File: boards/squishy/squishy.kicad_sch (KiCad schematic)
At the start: 66 parts, among them J10 QXH-060, J2 Conn_02x20_Odd_Even_Shielded, J8 TRIGGER, J9 REFCLK, SW2 DFU, U1 LFE5UM5G-45F-8BG381C, U2 GD25Q64EWIGR, U6 ATSAMD09D14A-M, X1 48MHz

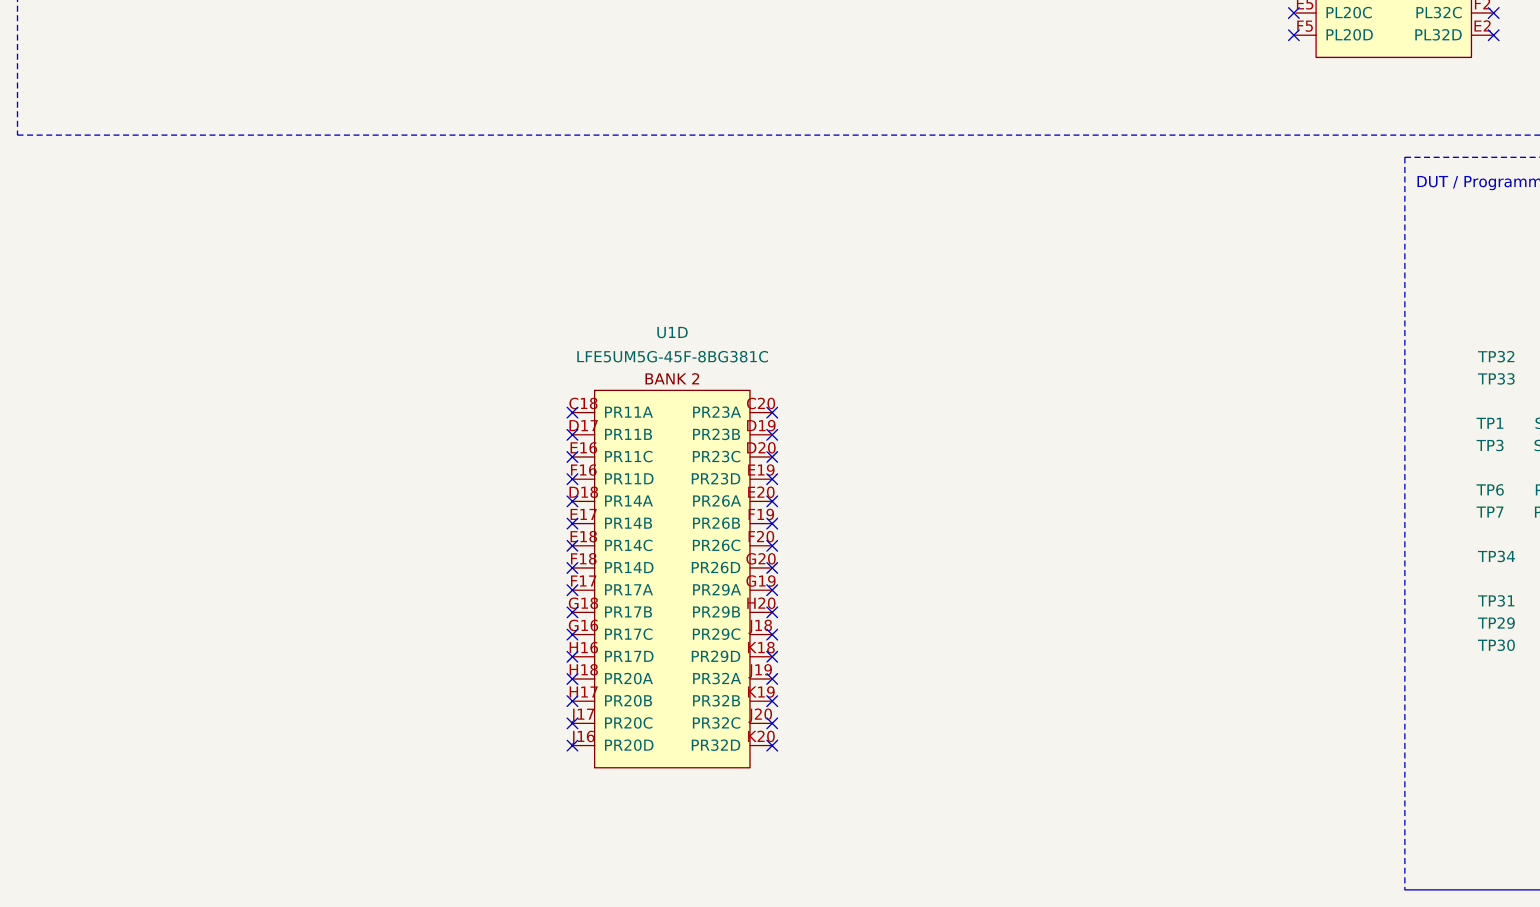
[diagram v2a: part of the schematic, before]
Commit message: hardware: squishy: added the microSD card slot
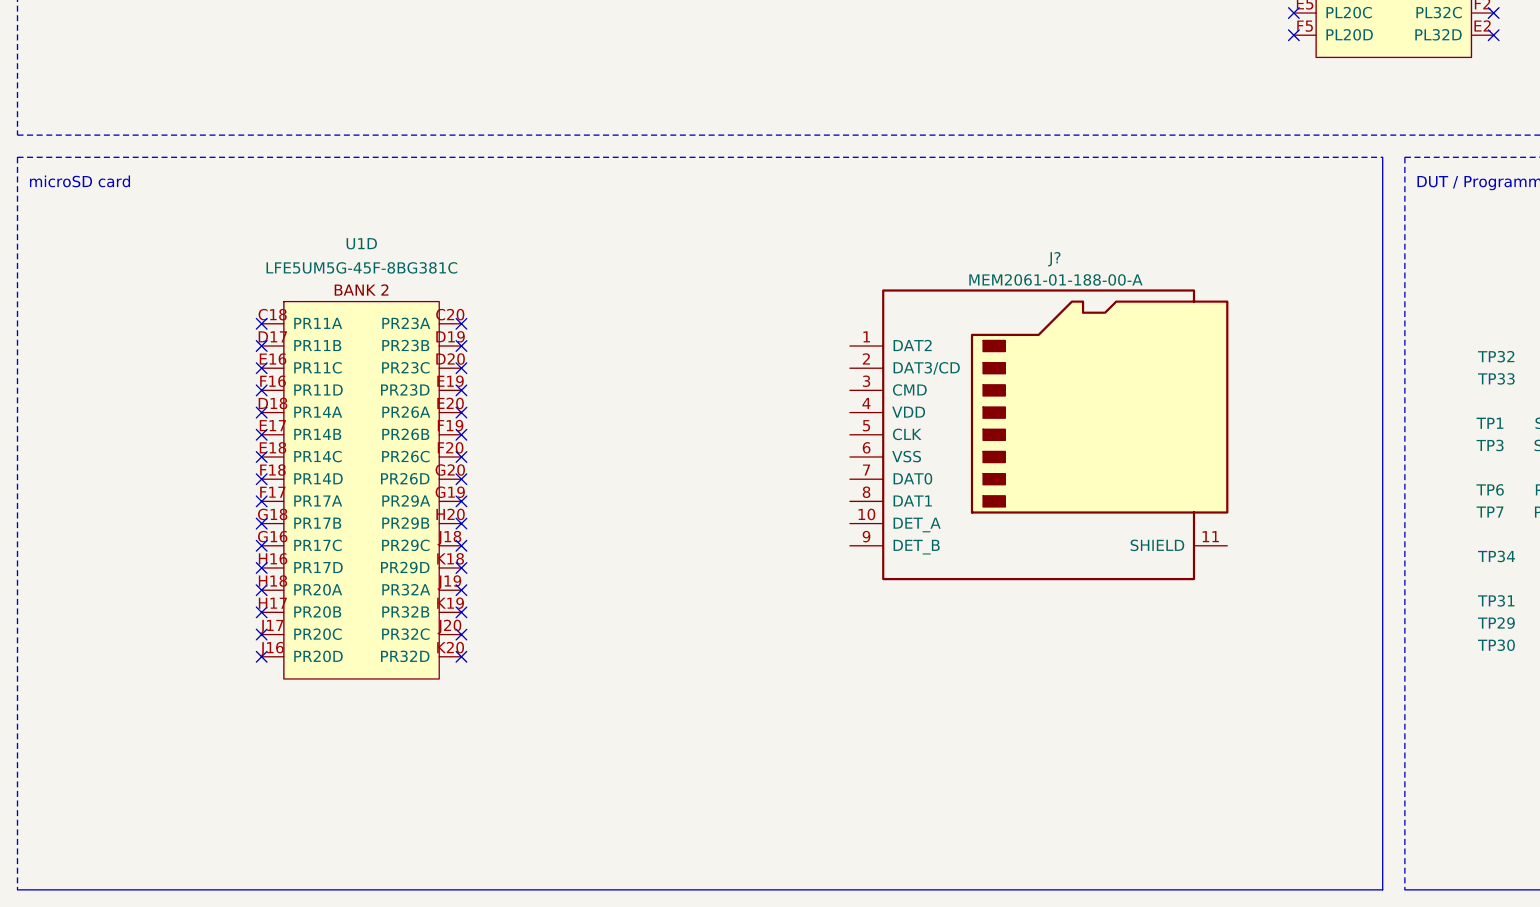
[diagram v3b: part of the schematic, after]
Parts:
- added J?: MEM2061-01-188-00-A, lethalbit-connectors:GCT_MEM2061-01-188-00-A_REVA, symbol Connector:Micro_SD_Card_Det
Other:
- note added: "microSD card"
- moved on the sheet: U1D
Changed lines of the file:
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@@
   (no_connect (at 290.83 93.98))
   (no_connect (at 290.83 78.74))
-  (no_connect (at 100.33 256.54))
-  (no_connect (at 100.33 254))
-  (no_connect (at 100.33 264.16))
-  (no_connect (at 100.33 261.62))
-  (no_connect (at 100.33 259.08))
-  (no_connect (at 77.47 254))
-  (no_connect (at 77.47 261.62))
-  (no_connect (at 77.47 256.54))
-  (no_connect (at 77.47 259.08))
-  (no_connect (at 77.47 251.46))
-  (no_connect (at 77.47 241.3))
-  (no_connect (at 77.47 243.84))
-  (no_connect (at 77.47 236.22))
-  (no_connect (at 77.47 231.14))
-  (no_connect (at 77.47 233.68))
-  (no_connect (at 77.47 238.76))
-  (no_connect (at 100.33 248.92))
-  (no_connect (at 100.33 251.46))
-  (no_connect (at 77.47 264.16))
-  (no_connect (at 100.33 246.38))
-  (no_connect (at 77.47 266.7))
-  (no_connect (at 77.47 228.6))
-  (no_connect (at 100.33 236.22))
-  (no_connect (at 100.33 231.14))
-  (no_connect (at 100.33 228.6))
-  (no_connect (at 100.33 243.84))
-  (no_connect (at 100.33 238.76))
-  (no_connect (at 100.33 241.3))
-  (no_connect (at 100.33 233.68))
-  (no_connect (at 77.47 246.38))
-  (no_connect (at 77.47 248.92))
+  (no_connect (at 64.77 246.38))
+  (no_connect (at 64.77 243.84))
+  (no_connect (at 64.77 254))
+  (no_connect (at 64.77 251.46))
+  (no_connect (at 64.77 248.92))
+  (no_connect (at 41.91 243.84))
+  (no_connect (at 41.91 251.46))
+  (no_connect (at 41.91 246.38))
+  (no_connect (at 41.91 248.92))
+  (no_connect (at 41.91 241.3))
+  (no_connect (at 41.91 231.14))
+  (no_connect (at 41.91 233.68))
+  (no_connect (at 41.91 226.06))
+  (no_connect (at 41.91 220.98))
+  (no_connect (at 41.91 223.52))
+  (no_connect (at 41.91 228.6))
+  (no_connect (at 64.77 238.76))
+  (no_connect (at 64.77 241.3))
+  (no_connect (at 41.91 254))
+  (no_connect (at 64.77 236.22))
+  (no_connect (at 41.91 256.54))
+  (no_connect (at 41.91 218.44))
+  (no_connect (at 64.77 226.06))
+  (no_connect (at 64.77 220.98))
+  (no_connect (at 64.77 218.44))
+  (no_connect (at 64.77 233.68))
+  (no_connect (at 64.77 228.6))
+  (no_connect (at 64.77 231.14))
+  (no_connect (at 64.77 223.52))
+  (no_connect (at 41.91 236.22))
+  (no_connect (at 41.91 238.76))
   (no_connect (at 215.9 153.67))
   (no_connect (at 215.9 168.91))
@@
   (no_connect (at 290.83 71.12))
   (no_connect (at 364.49 170.18))
-  (no_connect (at 100.33 266.7))
+  (no_connect (at 64.77 256.54))
   (no_connect (at 182.88 160.02))
   (no_connect (at 182.88 157.48))
@@
     (stroke (width 0) (type solid) (color 0 0 0 0))
   )
+  (polyline (pts (xy 170.18 283.21) (xy 170.18 199.39))
+    (stroke (width 0) (type default) (color 0 0 0 0))
+  )
   (polyline (pts (xy 265.43 114.3) (xy 406.4 114.3))
     (stroke (width 0) (type dash) (color 0 0 0 0))
@@
     (stroke (width 0) (type default) (color 0 0 0 0))
   )
+  (polyline (pts (xy 13.97 199.39) (xy 13.97 283.21))
+    (stroke (width 0) (type dash) (color 0 0 0 0))
+  )
   (wire (pts (xy 335.28 242.57) (xy 335.28 243.84))
     (stroke (width 0) (type default) (color 0 0 0 0))
@@
     (stroke (width 0) (type default) (color 0 0 0 0))
   )
+  (polyline (pts (xy 13.97 199.39) (xy 170.18 199.39))
+    (stroke (width 0) (type dash) (color 0 0 0 0))
+  )
   (wire (pts (xy 80.01 135.89) (xy 96.52 135.89))
     (stroke (width 0) (type default) (color 0 0 0 0))
@@
     (stroke (width 0) (type default) (color 0 0 0 0))
   )
+  (polyline (pts (xy 13.97 283.21) (xy 170.18 283.21))
+    (stroke (width 0) (type default) (color 0 0 0 0))
+  )
   (wire (pts (xy 306.07 43.18) (xy 306.07 45.72))
     (stroke (width 0) (type solid) (color 0 0 0 0))
@@
     (effects (font (size 1.27 1.27)) (justify right bottom))
   )
+  (text "microSD card" (at 15.24 203.2 0)
+    (effects (font (size 1.27 1.27)) (justify left bottom))
+  )
   (text "FPGA Core\n" (at 275.59 64.77 0)
     (effects (font (size 1.27 1.27)) (justify left bottom))
@@
     (pin "GND")
   )
+  (symbol (lib_id "Connector:Micro_SD_Card_Det") (at 132.08 231.14 0) (unit 1)
+    (in_bom yes) (on_board yes) (fields_autoplaced)
+    (property "Reference" "J?" (id 0) (at 132.715 210.9302 0))
+    (property "Value" "MEM2061-01-188-00-A" (id 1) (at 132.715 213.4671 0))
+    (property "Footprint" "lethalbit-connectors:GCT_MEM2061-01-188-00-A_REVA" (id 2) (at 184.15 213.36 0)
+      (effects (font (size 1.27 1.27)) hide)
+    )
+    (property "Datasheet" "https://gct.co/connector/digi-key/mem2061" (id 3) (at 132.08 228.6 0)
+      (effects (font (size 1.27 1.27)) hide)
+    )
+    (property "MFR" "GCT" (id 4) (at 132.08 231.14 0)
+      (effects (font (size 1.27 1.27)) hide)
+    )
+    (property "MPN" "MEM2061-01-188-00-A" (id 5) (at 132.08 231.14 0)
+      (effects (font (size 1.27 1.27)) hide)
+    )
+    (pin "1")
+    (pin "10")
+    (pin "11")
+    (pin "2")
+    (pin "3")
+    (pin "4")
+    (pin "5")
+    (pin "6")
+    (pin "7")
+    (pin "8")
+    (pin "9")
+  )
   (symbol (lib_id "Device:R_Small") (at 321.31 227.33 0) (unit 1)
     (in_bom yes) (on_board yes)
@@
     (pin "1")
   )
-  (symbol (lib_id "lethalbit:LFE5UM5G-45F-8BG381C") (at 88.9 228.6 0) (unit 4)
+  (symbol (lib_id "lethalbit:LFE5UM5G-45F-8BG381C") (at 53.34 218.44 0) (unit 4)
     (in_bom yes) (on_board yes)
-    (property "Reference" "U1" (id 0) (at 88.9 219.4749 0))
-    (property "Value" "LFE5UM5G-45F-8BG381C" (id 1) (at 88.9 222.25 0))
-    (property "Footprint" "lethalbit:318caBGA" (id 2) (at 88.9 213.36 0)
+    (property "Reference" "U1" (id 0) (at 53.34 209.3149 0))
+    (property "Value" "LFE5UM5G-45F-8BG381C" (id 1) (at 53.34 212.09 0))
+    (property "Footprint" "lethalbit:318caBGA" (id 2) (at 53.34 203.2 0)
       (effects (font (size 1.27 1.27)) hide)
     )
-    (property "Datasheet" "https://www.latticesemi.com/view_document?document_id=50461" (id 3) (at 88.9 275.59 0)
+    (property "Datasheet" "https://www.latticesemi.com/view_document?document_id=50461" (id 3) (at 53.34 265.43 0)
       (effects (font (size 1.27 1.27)) hide)
     )
-    (property "MFR" "Lattice" (id 4) (at 88.9 215.9 0)
+    (property "MFR" "Lattice" (id 4) (at 53.34 205.74 0)
       (effects (font (size 1.27 1.27)) hide)
     )
-    (property "MPN" "LFE5UM5G-45F-8BG381C" (id 5) (at 88.9 219.71 0)
+    (property "MPN" "LFE5UM5G-45F-8BG381C" (id 5) (at 53.34 209.55 0)
       (effects (font (size 1.27 1.27)) hide)
     )
@@
       (reference "J10") (unit 4) (value "QXH-060") (footprint "lethalbit-connectors:QTH-060-01-X-D-RA-PGP")
     )
+    (path "/7eb154ec-8fa5-45f8-8bb2-1af652de1111"
+      (reference "J?") (unit 1) (value "MEM2061-01-188-00-A") (footprint "lethalbit-connectors:GCT_MEM2061-01-188-00-A_REVA")
+    )
     (path "/de707440-a3c6-4b49-832e-b7263045abb4/81f65ea4-a4dc-47d7-9ed4-032499b665e0"

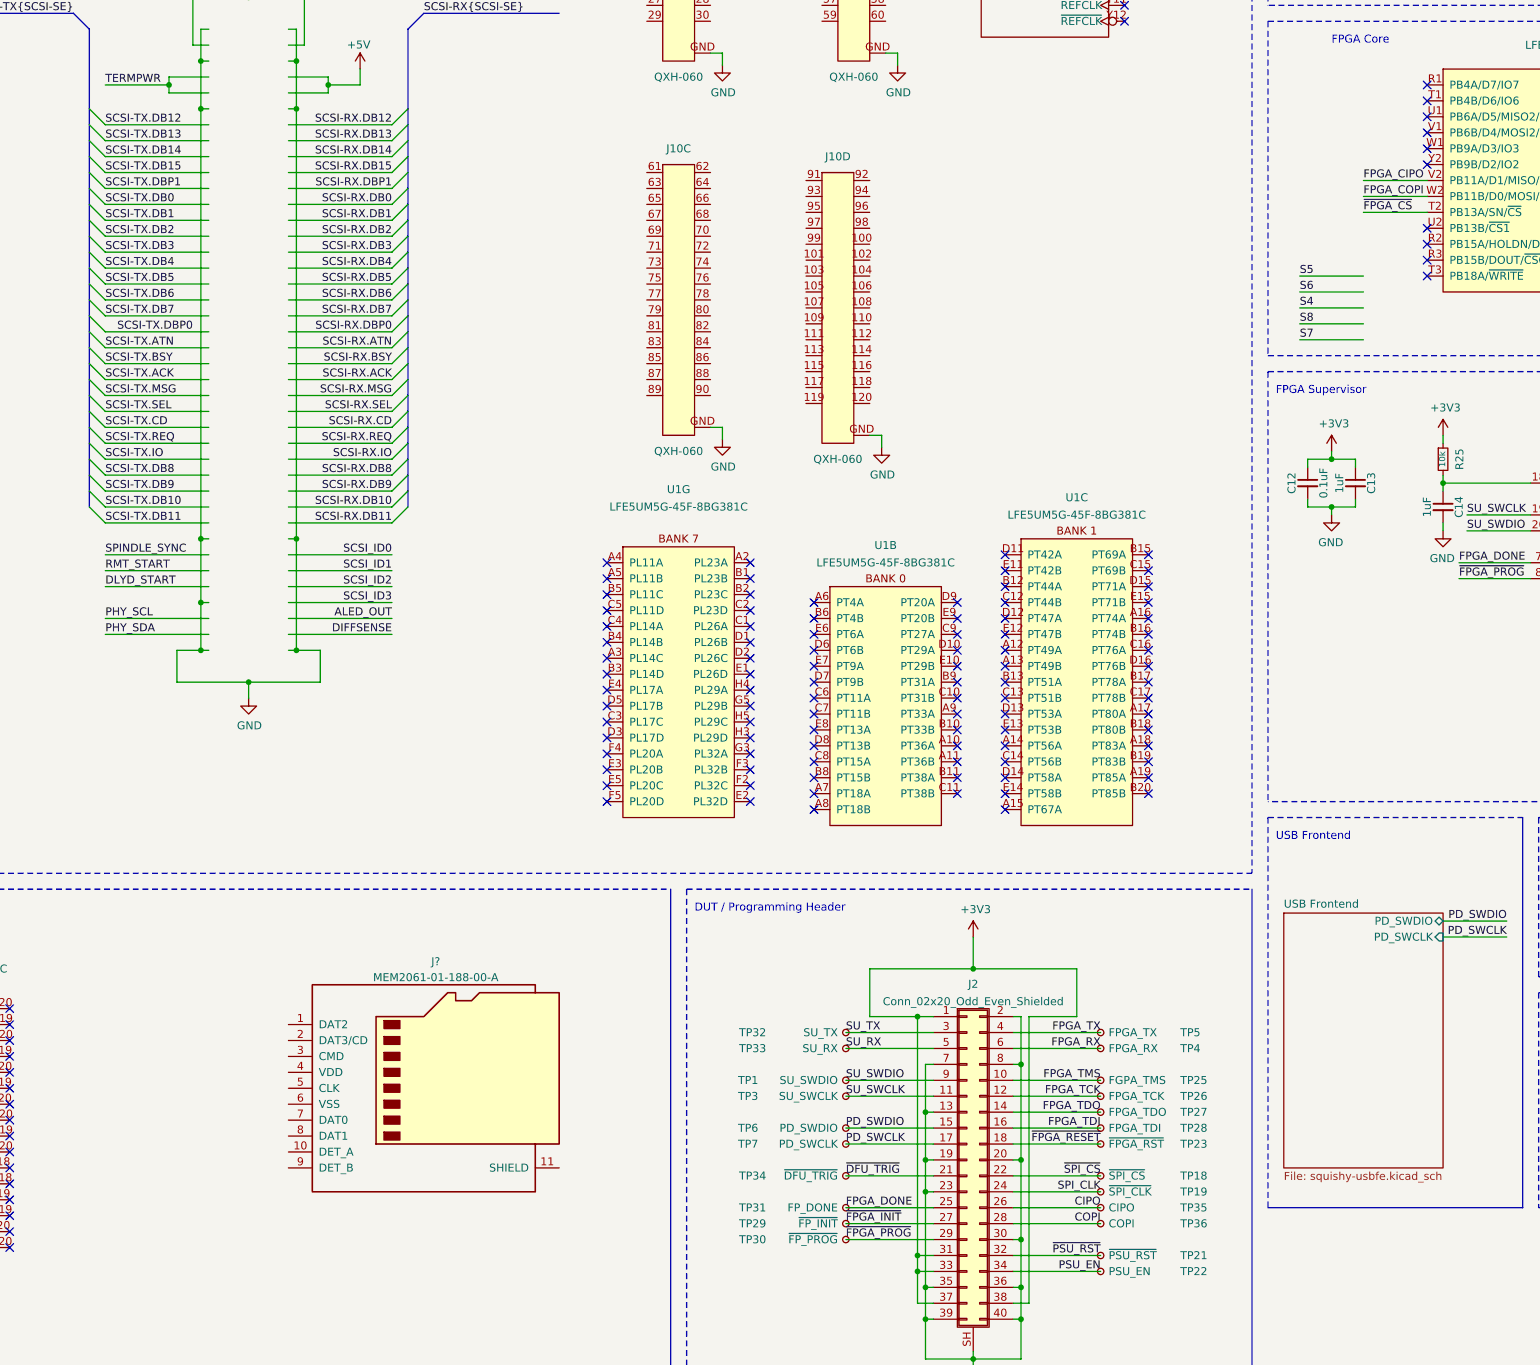
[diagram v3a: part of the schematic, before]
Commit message: hardware: squishy: some misc additions, mainly a pull-up resistor for the sd card detect and the SPI CS for the FPGA
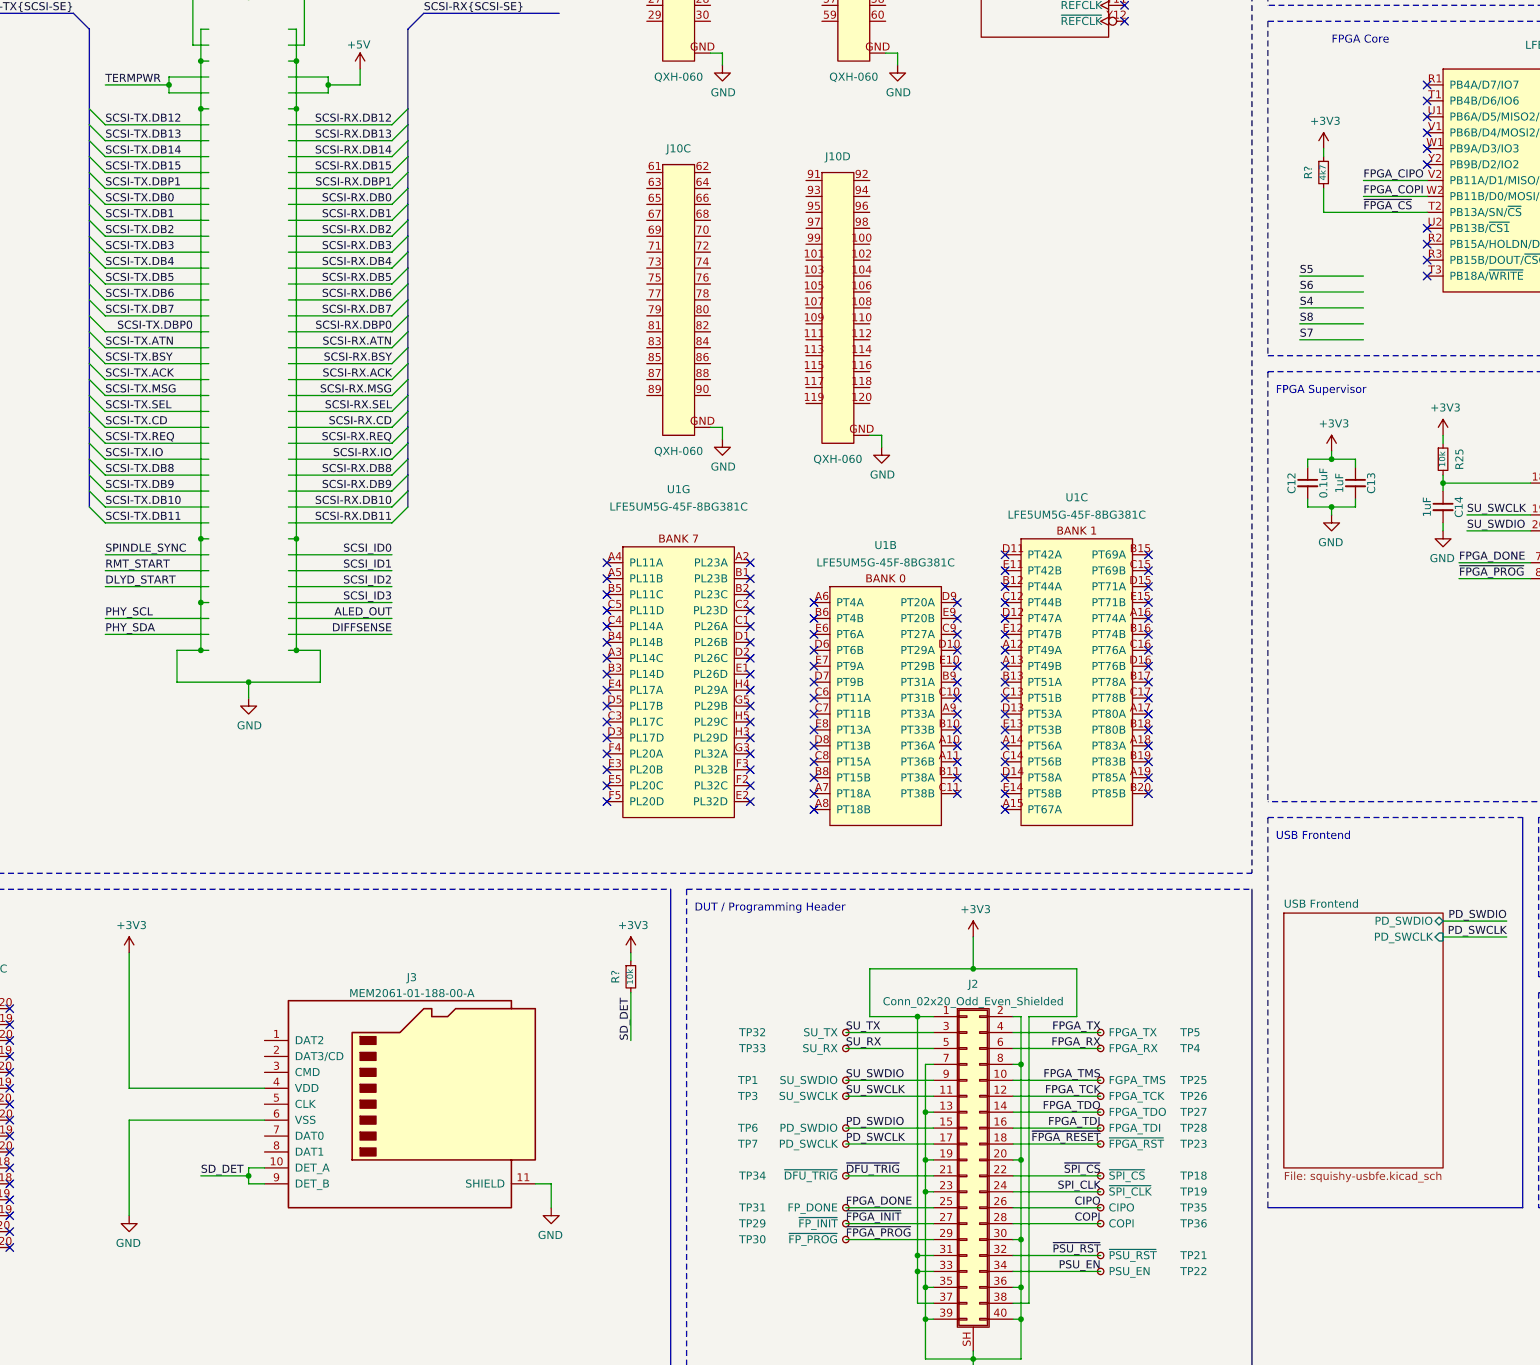
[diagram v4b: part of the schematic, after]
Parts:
- added R?: 10k, Resistor_SMD:R_0603_1608Metric, symbol Device:R_Small
- added R?: 4k7, Resistor_SMD:R_0603_1608Metric, symbol Device:R_Small
- gave numbers to parts that had none: 1
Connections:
- net +3V3: now also J3.4 (VDD), R?.1, R?.1
- net GND: now also J3.11 (SHIELD), J3.6 (VSS)
- net ~{FPGA_CS}: now also R?.2
- net SD_DET: now reaches J3.10 (DET_A)
- net SD_DET: now also J3.9 (DET_B), R?.2
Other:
- moved on the sheet: J3
